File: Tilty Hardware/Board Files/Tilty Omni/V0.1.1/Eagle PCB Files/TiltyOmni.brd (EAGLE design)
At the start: 41.9 x 52.1 mm, 36 parts, among them U1 TEENSY_3.0_ALLPINSTEENSY_3.0_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, U2 HC-09_BREAKOUT, U4 LM2931, U5 MPU-6050, U7 SPI_FLASH-X25XXSMD

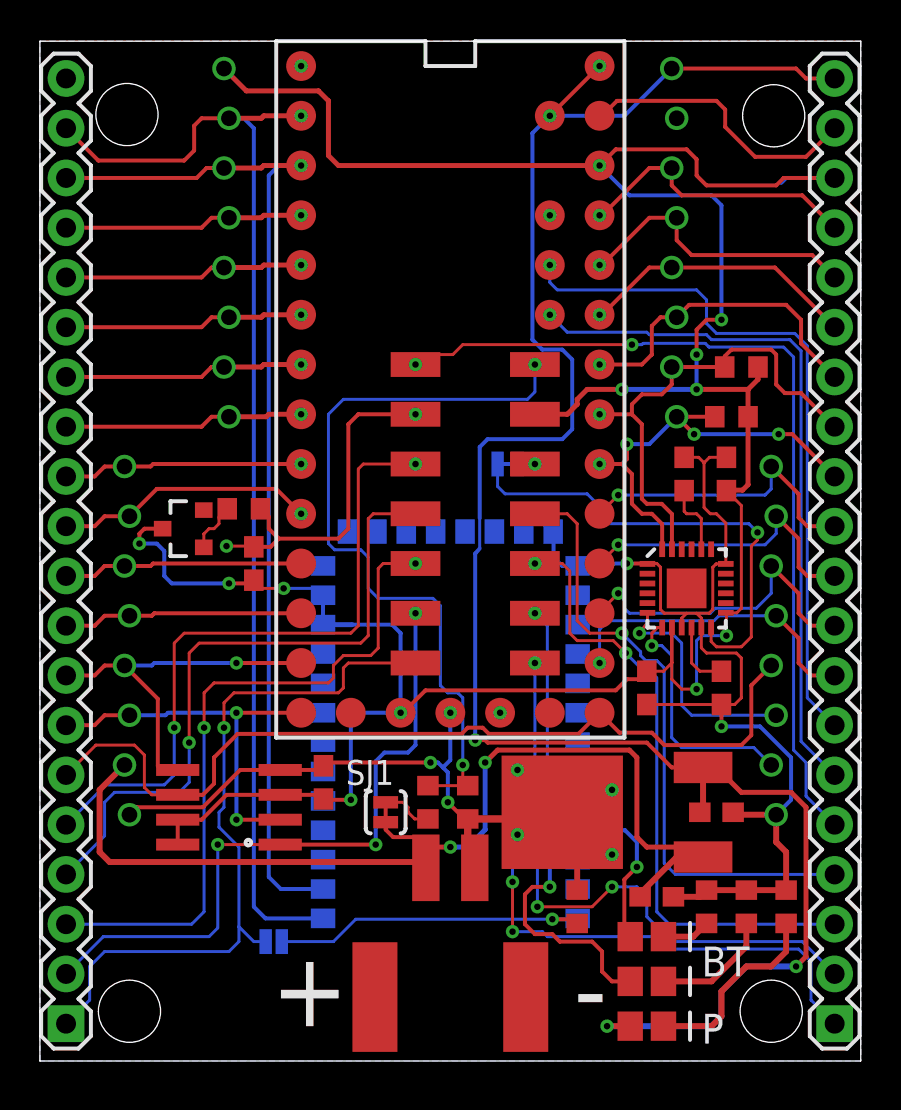
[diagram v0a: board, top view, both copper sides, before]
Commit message: Removed some excess soldermask keepout on Dual Motor Driver, prototype review of Tilty Omni
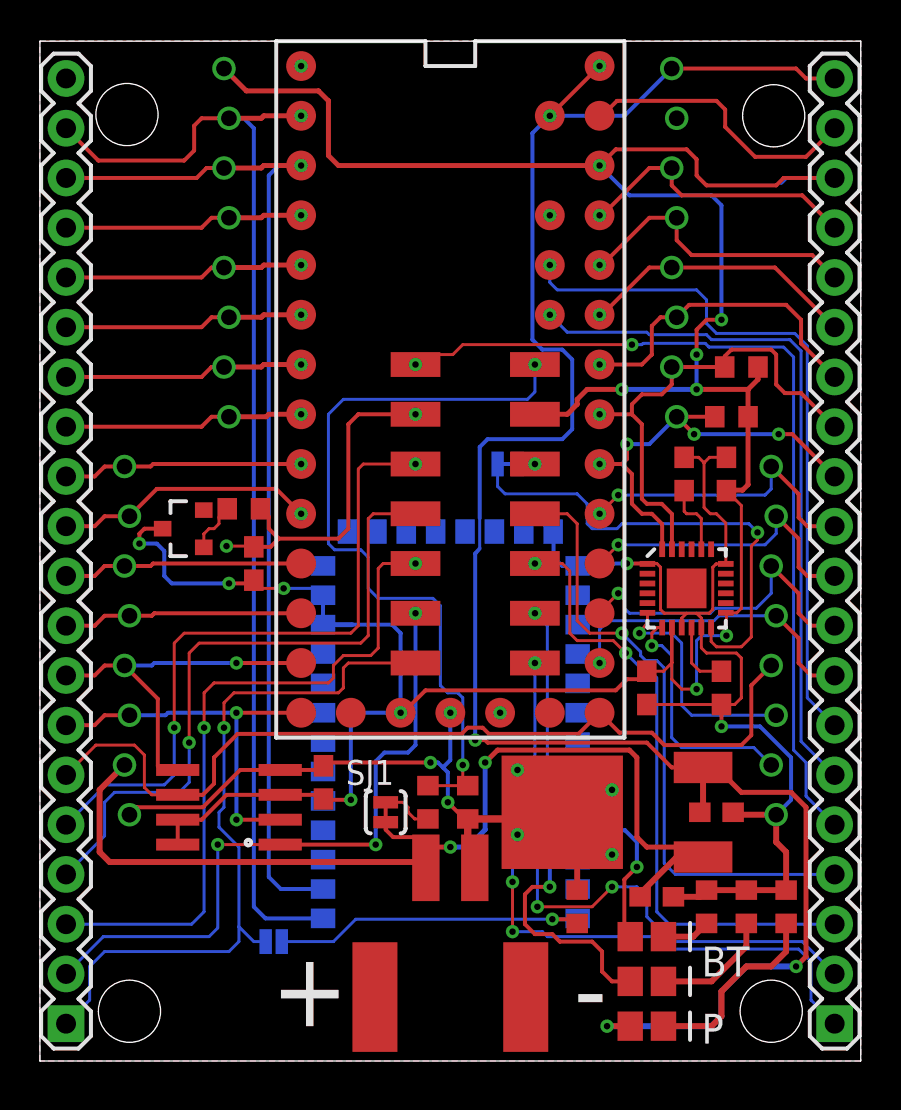
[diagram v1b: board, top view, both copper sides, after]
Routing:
- net N$16: track 24.2 -> 24.7 mm
- net 5V_SDA: vias 1 -> 2
- added copper zone on layer 1, net N$6
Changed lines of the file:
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@@
 <wire x1="36.6395" y1="26.6065" x2="36.322" y2="26.289" width="0.1524" layer="1"/>
 <wire x1="36.322" y1="26.289" x2="36.322" y2="21.6535" width="0.1524" layer="1"/>
-<wire x1="23.749" y1="28.956" x2="27.94" y2="28.956" width="0.1524" layer="16"/>
-<wire x1="27.94" y1="28.956" x2="28.448" y2="28.448" width="0.1524" layer="16"/>
-<wire x1="28.448" y1="28.448" x2="28.448" y2="27.94" width="0.1524" layer="16"/>
-<wire x1="28.448" y1="27.94" x2="28.956" y2="27.432" width="0.1524" layer="16"/>
-<wire x1="28.956" y1="27.432" x2="36.195" y2="27.432" width="0.1524" layer="16"/>
+<wire x1="23.749" y1="28.956" x2="27.432" y2="28.956" width="0.1524" layer="16"/>
+<wire x1="29.718" y1="27.432" x2="36.195" y2="27.432" width="0.1524" layer="16"/>
 <wire x1="23.749" y1="28.956" x2="23.368" y2="29.337" width="0.1524" layer="16"/>
 <wire x1="23.368" y1="29.337" x2="23.368" y2="30.48" width="0.1524" layer="16"/>
+<wire x1="29.718" y1="27.432" x2="29.464" y2="27.178" width="0.1524" layer="16"/>
+<wire x1="29.464" y1="27.178" x2="28.194" y2="27.178" width="0.1524" layer="16"/>
+<wire x1="28.194" y1="27.178" x2="27.94" y2="27.432" width="0.1524" layer="16"/>
+<wire x1="27.94" y1="27.432" x2="27.94" y2="28.448" width="0.1524" layer="16"/>
+<wire x1="27.94" y1="28.448" x2="27.432" y2="28.956" width="0.1524" layer="16"/>
 </signal>
 <signal name="BT_CMD">
@@
 <wire x1="38.735" y1="27.7495" x2="38.735" y2="28.956" width="0.2032" layer="1"/>
 <wire x1="38.735" y1="28.956" x2="37.338" y2="30.353" width="0.2032" layer="1"/>
+<via x="28.575" y="27.94" extent="1-16" drill="0.3302"/>
 </signal>
 <signal name="5V_SCL">
@@
 <via x="23.495" y="17.78" extent="1-16" drill="0.3302"/>
 </signal>
+<signal name="N$6">
+<polygon width="0.1524" layer="1">
+<vertex x="0" y="52.07"/>
+<vertex x="41.91" y="52.07"/>
+<vertex x="41.91" y="0"/>
+<vertex x="0" y="0"/>
+</polygon>
+</signal>
 </signals>

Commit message: Modified random experiment program to test new motor driver
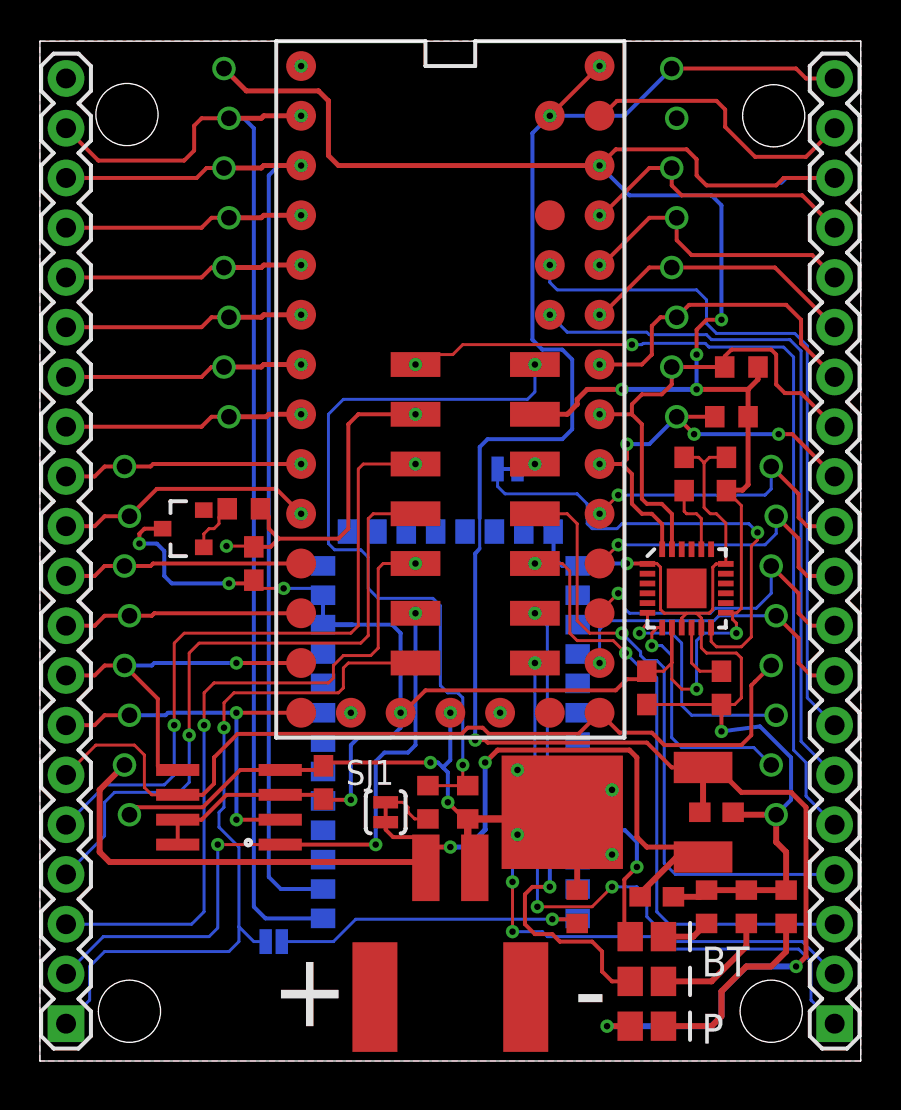
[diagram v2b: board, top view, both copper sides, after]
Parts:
- moved MPU_INT 0.25 mm to (23.9, 30.2)
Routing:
- net +3V3: track 149.7 -> 150.2 mm
